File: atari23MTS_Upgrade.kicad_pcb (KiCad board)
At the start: 2 copper layers, 136 x 88 mm, 54 parts, among them P1 CONN_01X01, P2 CONN_01X01, P3 CONN_01X01, P4 CONN_01X01, P5 CONN_01X01, SW1 SW_PUSH, U1 NCP1117ST33T3G, U10 TXB0108-PW, U11 ISSI61WV5128BL, U12 ISSI61WV5128BL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

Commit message: Revised logic using nOE and R/nW as supposed to be...
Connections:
- U11 pad 24: ~ADDRESS_SELECTOR -> ~mOE
- U12 pad 24: ~ADDRESS_SELECTOR -> ~mOE
- U13 pad 24: ~ADDRESS_SELECTOR -> ~mOE
- U14 pad 24: ~ADDRESS_SELECTOR -> ~mOE
- U3 pad 4: Net-(U3-Pad4) -> ~ADDRSEL16K
- U3 pad 5: Net-(U3-Pad4) -> ~ADDRSEL16K
- U7 pad 3: (no net) -> mR/~W
- U7 pad 4: (no net) -> ~mOE
- U9 pad 3: ~ADDRESS_SELECTOR -> ~ADDRSEL16K
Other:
- board text added: "GND RX TX"

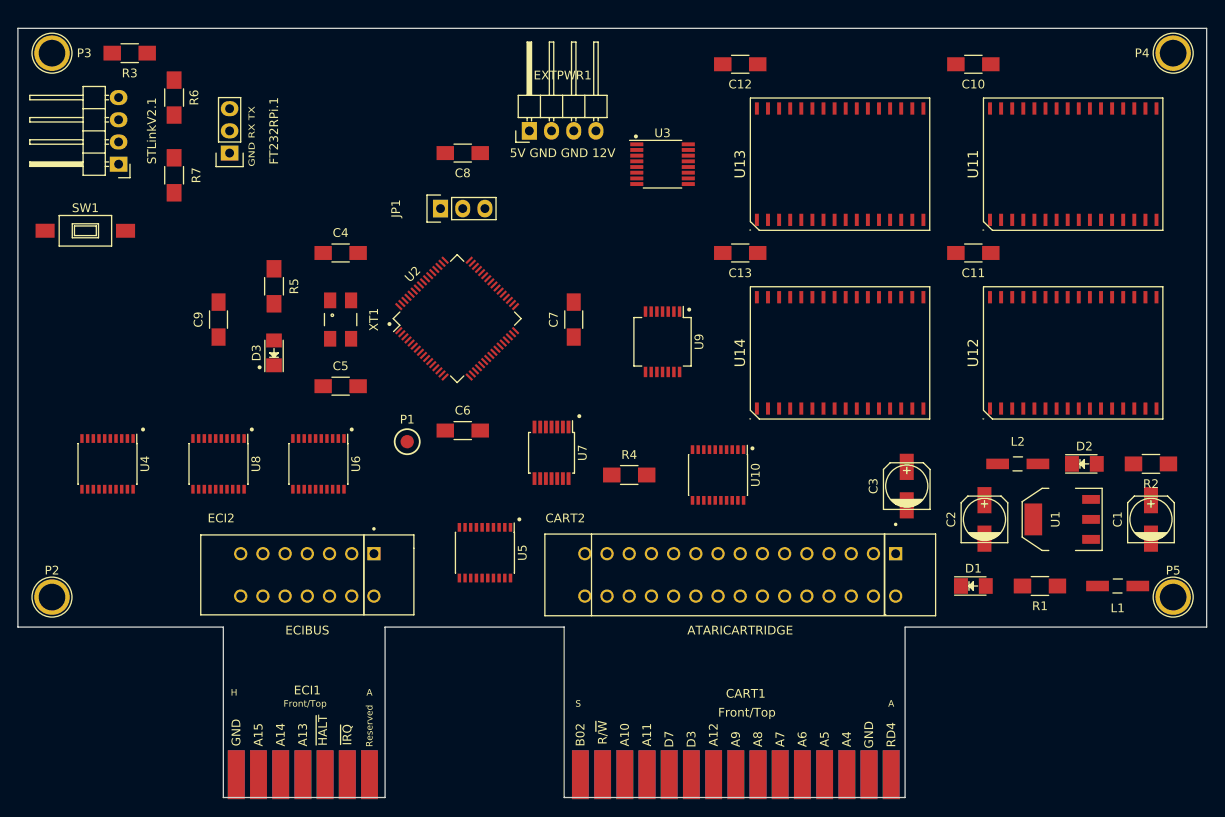
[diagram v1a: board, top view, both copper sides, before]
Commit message: Added the passthru for Cartridge and ECI bus
Added the passthru for Cartridge and ECI bus and moved
some components for better autorouting for FreeRoute
Next step is to use the better rule for trace length (Kicad or
FreeRoute?)
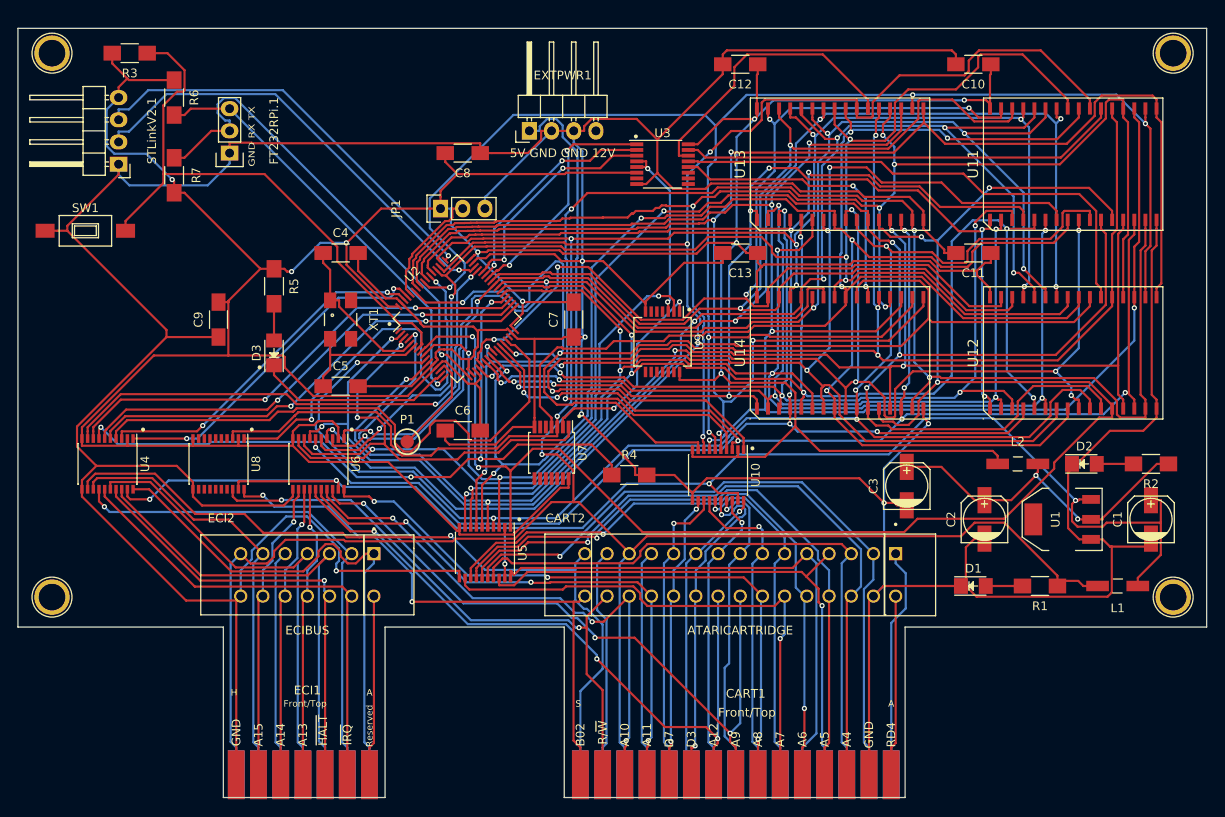
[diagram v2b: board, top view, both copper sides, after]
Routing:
- net GND: track 0.00 -> 665.2 mm, vias 0 -> 6
- net VCC3V3: track 0.00 -> 492.5 mm, vias 0 -> 9
- net mA10: track 0.00 -> 227.9 mm, vias 0 -> 4
- net +5VDC: track 0.00 -> 214.8 mm, vias 0 -> 1
- net mA12: track 0.00 -> 195.5 mm, vias 0 -> 6
- net mA0: track 0.00 -> 194.7 mm, vias 0 -> 5
- net mD4: track 0.00 -> 192.4 mm, vias 0 -> 5
- net mD5: track 0.00 -> 191.3 mm, vias 0 -> 5
- net mA1: track 0.00 -> 189.5 mm, vias 0 -> 6
- net mD3: track 0.00 -> 183.6 mm, vias 0 -> 4
- net mR/~W: track 0.00 -> 181.6 mm, vias 0 -> 7
- net mD7: track 0.00 -> 178.8 mm, vias 0 -> 5
- net mA2: track 0.00 -> 178.1 mm, vias 0 -> 5
- net VCC5V: track 0.00 -> 172.2 mm, vias 0 -> 5
- net mA11: track 0.00 -> 170.3 mm, vias 0 -> 5
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
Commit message: Added logos & GND Pin for electrical debugging
Added Atari Logo on the back
Added GNU GPL on Silkscreen Top
Added Test Point for GROUND (do not place in production)
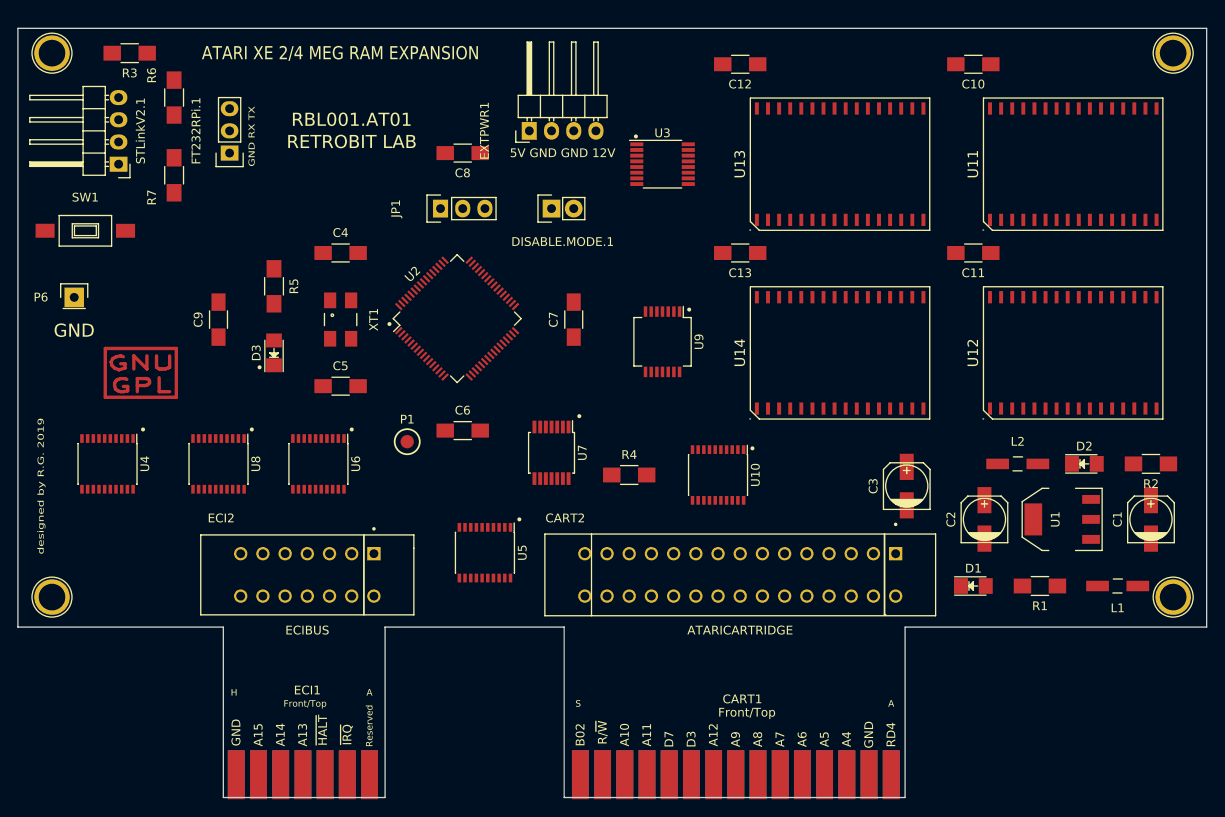
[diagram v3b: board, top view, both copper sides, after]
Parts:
- added DISABLE.MODE.1: CONN_01X02, Pin_Headers:Pin_Header_Straight_1x02, F.Cu at (146.1, 71.1)
- added LOGO: LOGO, RetroBitLab:atari_fuji_SilkScreen_21.2x25-RevBack, B.Cu at (153.7, 86.4)
- added P6: CONN_01X01, Pin_Headers:Pin_Header_Straight_1x01, F.Cu at (91.4, 81.3)
- added REF**: Symbol_GNU-GPL_CopperTop_Small, Symbols:Symbol_GNU-GPL_CopperTop_Small, F.Cu at (99.1, 90.2)
- CART1: footprint RetroBitLab:ATARI-LEFT-CARTRIDGE -> ATARI-LEFT-CARTRIDGE
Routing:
- net GND: track 665.2 -> 0.00 mm, vias 6 -> 0
- net VCC3V3: track 492.5 -> 0.00 mm, vias 9 -> 0
- net mA10: track 227.9 -> 0.00 mm, vias 4 -> 0
- net +5VDC: track 214.8 -> 0.00 mm, vias 1 -> 0
- net mA12: track 195.5 -> 0.00 mm, vias 6 -> 0
- net mA0: track 194.7 -> 0.00 mm, vias 5 -> 0
- net mD4: track 192.4 -> 0.00 mm, vias 5 -> 0
- net mD5: track 191.3 -> 0.00 mm, vias 5 -> 0
- net mA1: track 189.5 -> 0.00 mm, vias 6 -> 0
- net mD3: track 183.6 -> 0.00 mm, vias 4 -> 0
- net mR/~W: track 181.6 -> 0.00 mm, vias 7 -> 0
- net mD7: track 178.8 -> 0.00 mm, vias 5 -> 0
- net mA2: track 178.1 -> 0.00 mm, vias 5 -> 0
- net VCC5V: track 172.2 -> 0.00 mm, vias 5 -> 0
- net mA11: track 170.3 -> 0.00 mm, vias 5 -> 0
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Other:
- net class Default: via_dia 0.6 -> 0.4; via_drill 0.4 -> 0.3
- board text added: "8-BIT"
- board text added: "ATARI XE 2/4 MEG RAM EXPANSION"
- board text added: "GND"
- board text added: "Power Without the Price!"
- board text added: "RBL001.AT01"
- board text added: "RETROBIT LAB"
- board text added: "designed by R.G. 2019"
- board text added: "in memoriam A.S.-G.D."

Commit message: Rebuilt with reset jumpers
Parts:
- moved REF** 10.5 mm to (101.6, 80.0)
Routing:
- net GND: track 0.00 -> 630.1 mm, vias 0 -> 6
- net VCC3V3: track 0.00 -> 417.3 mm, vias 0 -> 13
- net +5VDC: track 0.00 -> 215.5 mm, vias 0 -> 1
- net mR/~W: track 0.00 -> 193.5 mm, vias 0 -> 9
- net mD3: track 0.00 -> 190.0 mm, vias 0 -> 6
- net mD6: track 0.00 -> 182.9 mm, vias 0 -> 6
- net mA11: track 0.00 -> 181.4 mm, vias 0 -> 6
- net mA10: track 0.00 -> 175.8 mm, vias 0 -> 6
- net mD7: track 0.00 -> 171.7 mm, vias 0 -> 6
- net mA0: track 0.00 -> 170.9 mm, vias 0 -> 4
- net mA13: track 0.00 -> 170.9 mm, vias 0 -> 7
- net mD5: track 0.00 -> 170.7 mm, vias 0 -> 5
- net mD4: track 0.00 -> 169.7 mm, vias 0 -> 7
- net VCC5V: track 0.00 -> 167.9 mm, vias 0 -> 6
- net mD0: track 0.00 -> 165.4 mm, vias 0 -> 3
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- added copper zone on B.Cu, net GND

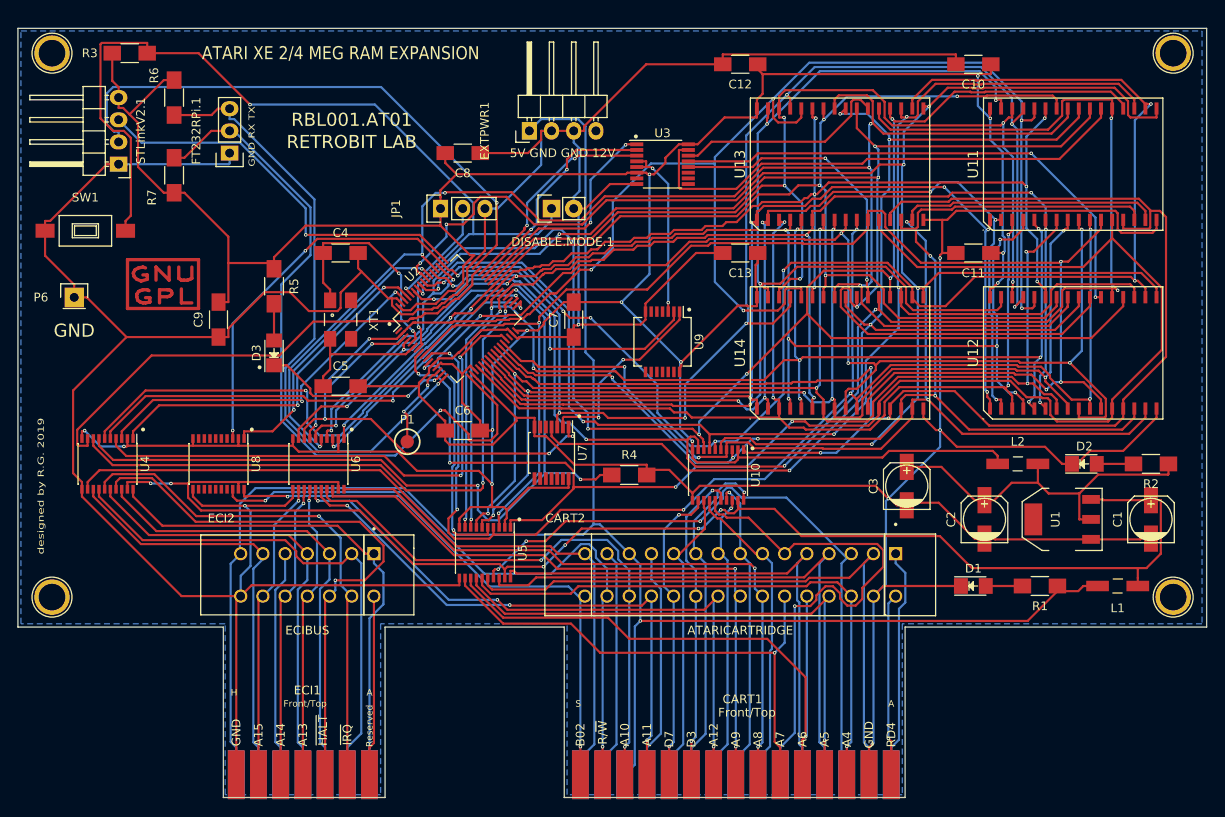
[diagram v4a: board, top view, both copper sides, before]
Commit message: Changed the bankselection $D530 and bankcontrol $D531
Changed the bankselection $D530 and bankcontrol $D531
Now in this way, only nCCTL can be used as address selector and only low
byte address is needed in the SoC
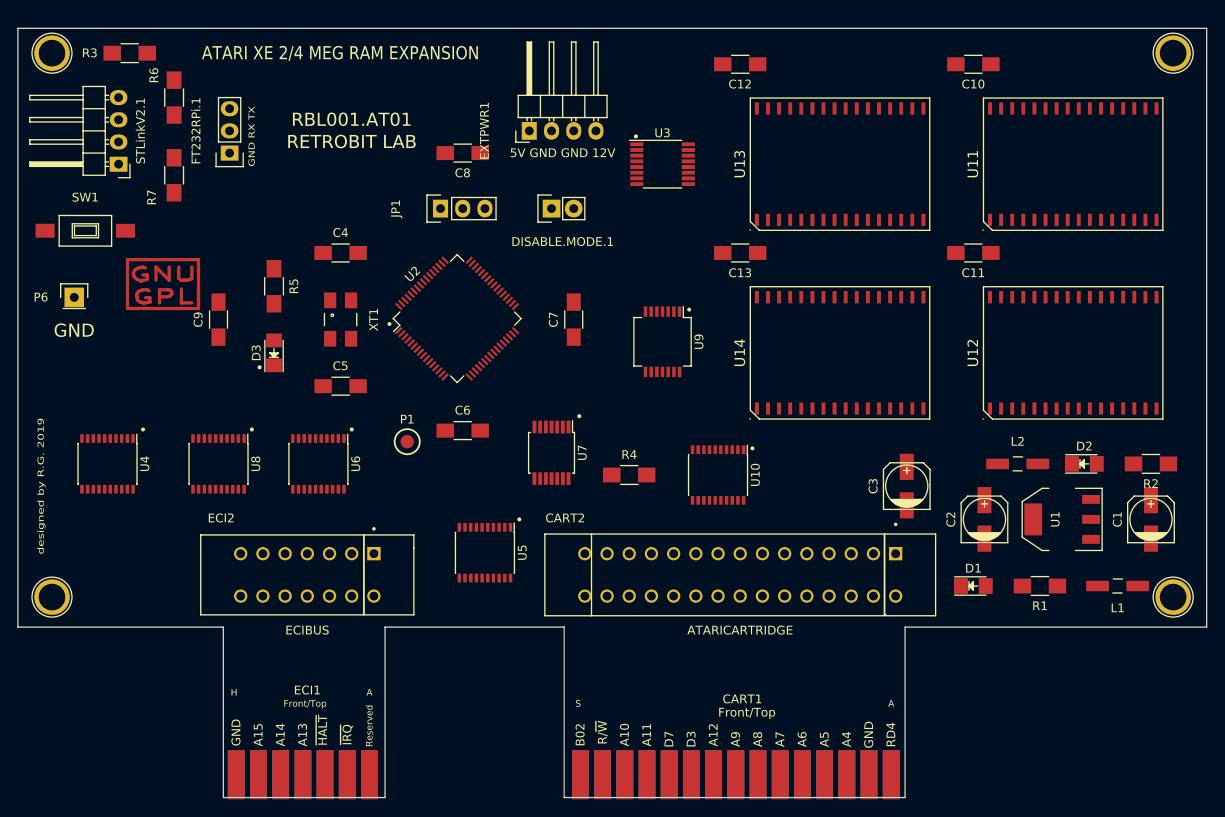
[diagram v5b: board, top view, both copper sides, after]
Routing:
- net GND: track 630.1 -> 0.00 mm, vias 6 -> 0
- net VCC3V3: track 417.3 -> 0.00 mm, vias 13 -> 0
- net +5VDC: track 215.5 -> 0.00 mm, vias 1 -> 0
- net mR/~W: track 193.5 -> 0.00 mm, vias 9 -> 0
- net mD3: track 190.0 -> 0.00 mm, vias 6 -> 0
- net mD6: track 182.9 -> 0.00 mm, vias 6 -> 0
- net mA11: track 181.4 -> 0.00 mm, vias 6 -> 0
- net mA10: track 175.8 -> 0.00 mm, vias 6 -> 0
- net mD7: track 171.7 -> 0.00 mm, vias 6 -> 0
- net mA0: track 170.9 -> 0.00 mm, vias 4 -> 0
- net mA13: track 170.9 -> 0.00 mm, vias 7 -> 0
- net mD5: track 170.7 -> 0.00 mm, vias 5 -> 0
- net mD4: track 169.7 -> 0.00 mm, vias 7 -> 0
- net VCC5V: track 167.9 -> 0.00 mm, vias 6 -> 0
- net mD0: track 165.4 -> 0.00 mm, vias 3 -> 0
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- removed copper zone on B.Cu, net GND

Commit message: Updated after new vias & tracks
Updated after new vias & tracks
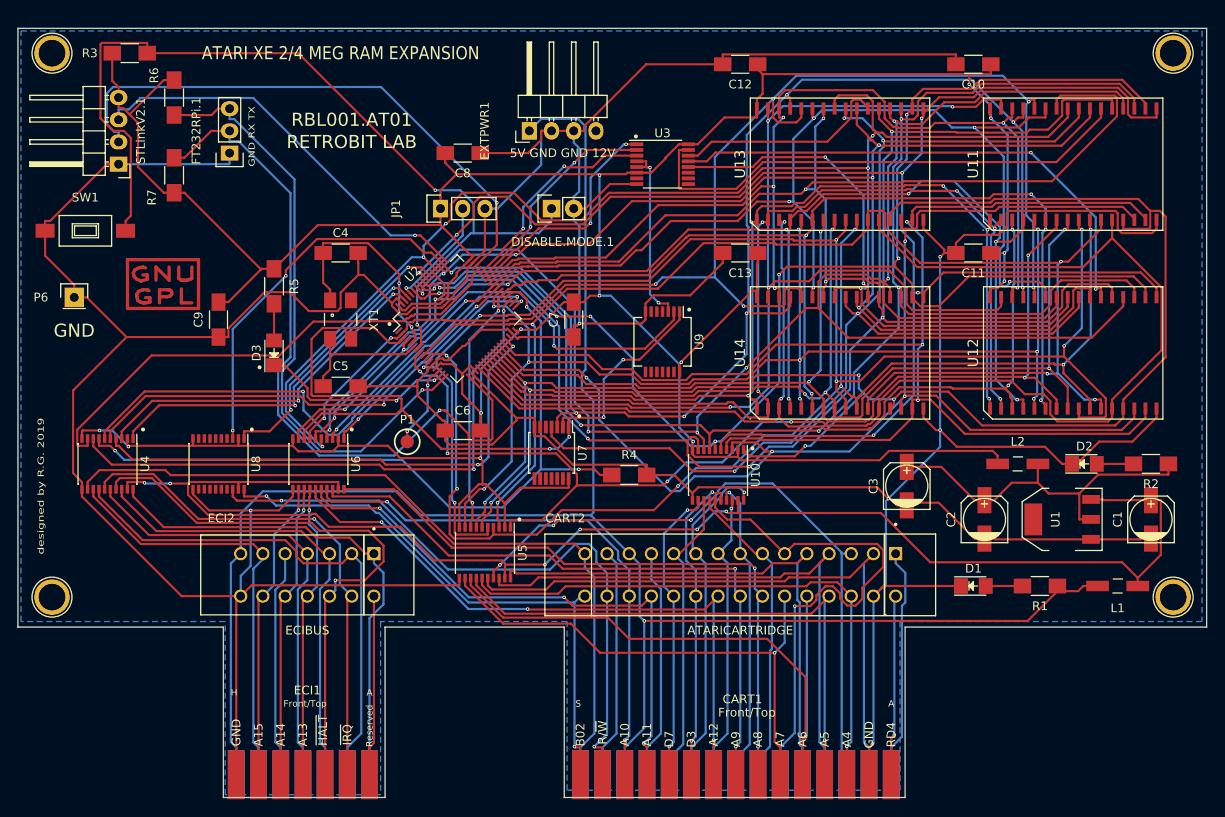
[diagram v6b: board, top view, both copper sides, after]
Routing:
- net GND: track 0.00 -> 629.2 mm, vias 0 -> 6
- net VCC3V3: track 0.00 -> 411.0 mm, vias 0 -> 13
- net +5VDC: track 0.00 -> 212.8 mm, vias 0 -> 1
- net mR/~W: track 0.00 -> 188.7 mm, vias 0 -> 9
- net mD3: track 0.00 -> 186.8 mm, vias 0 -> 6
- net mA11: track 0.00 -> 178.4 mm, vias 0 -> 6
- net mD6: track 0.00 -> 176.3 mm, vias 0 -> 6
- net mA9: track 0.00 -> 170.3 mm, vias 0 -> 5
- net mA0: track 0.00 -> 170.0 mm, vias 0 -> 4
- net mD7: track 0.00 -> 169.5 mm, vias 0 -> 5
- net mD5: track 0.00 -> 168.4 mm, vias 0 -> 5
- net VCC5V: track 0.00 -> 167.8 mm, vias 0 -> 6
- net mD4: track 0.00 -> 165.7 mm, vias 0 -> 7
- net mA10: track 0.00 -> 164.4 mm, vias 0 -> 6
- net mD0: track 0.00 -> 161.6 mm, vias 0 -> 3
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- added copper zone on B.Cu, net GND
